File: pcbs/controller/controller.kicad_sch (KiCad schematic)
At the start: 4 parts, among them J1 Conn_01x11, J2 Conn_01x02, J3 Conn_01x02, U1 XIAO-nRF52840-SMD

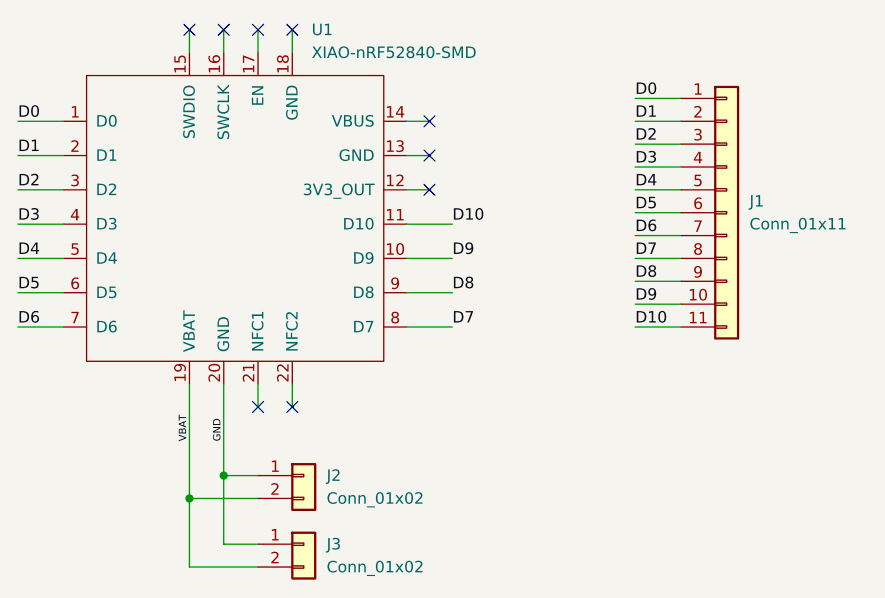
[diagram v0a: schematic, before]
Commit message: Route the controller board
Power on B.Cu (0.5 mm): J2 / J3 to the XIAO battery pads (U1-19 VBAT,
U1-20 GND), clear of B.Cu keepout rule areas (r 3) for the lid
pedestals under H1-H4.

Signals on F.Cu (0.25 mm), all single layer. The H1 screw head blocks
the outside of the top three left pins, and the B.Cu power traces cross
under the XIAO, so D0-D2 run under the module and enter J1 from behind.
D3-D6 and D7-D10 run outside the XIAO and enter J1 from the front,
under the connector body. J1 is reassigned to suit: pins 1-11 =
D6 D5 D4 D3 D2 D1 D0 D10 D9 D8 D7, so with a straight cable
D0-D6 = C0-C6 and D7-D10 = R0-R3.

Also reapply the controller Edge.Cuts after the 6.25-degree tilt
change.

Co-Authored-By: Claude Opus 5.5 <noreply@anthropic.com>
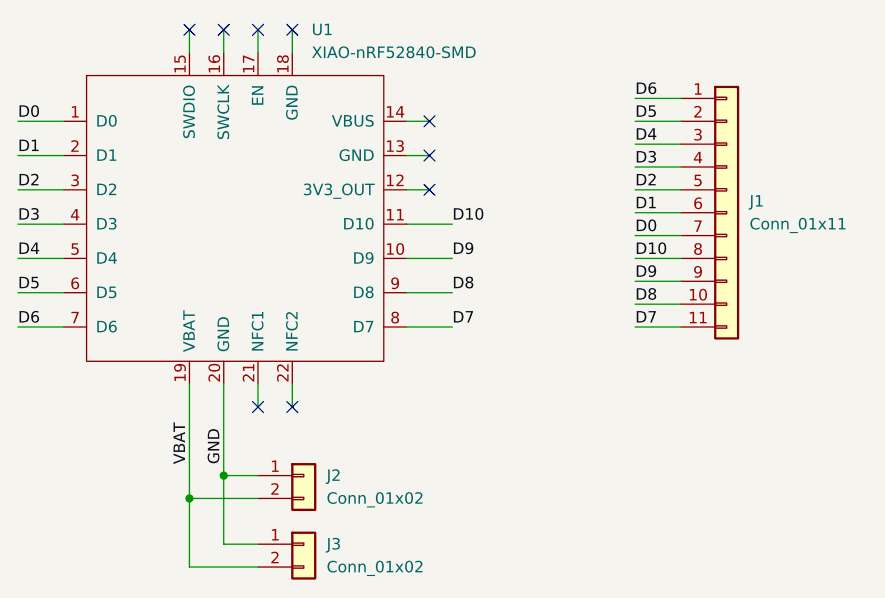
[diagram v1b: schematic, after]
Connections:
- net D0: now also J1.7 (Pin_7); no longer J1.1 (Pin_1)
- net D1: now also J1.6 (Pin_6); no longer J1.2 (Pin_2)
- net D10: now also J1.8 (Pin_8); no longer J1.11 (Pin_11)
- net D2: now also J1.5 (Pin_5); no longer J1.3 (Pin_3)
- net D4: now also J1.3 (Pin_3); no longer J1.5 (Pin_5)
- net D5: now also J1.2 (Pin_2); no longer J1.6 (Pin_6)
- net D6: now also J1.1 (Pin_1); no longer J1.7 (Pin_7)
- net D7: now also J1.11 (Pin_11); no longer J1.8 (Pin_8)
- net D8: now also J1.10 (Pin_10); no longer J1.9 (Pin_9)
- net D9: now also J1.9 (Pin_9); no longer J1.10 (Pin_10)
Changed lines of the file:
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@@
+		)
+	)
+	(label "GND"
+		(at 60.96 90.17 90)
+		(effects
+			(font
+				(size 1.27 1.27)
+			)
+			(justify left bottom)
 		)
 	)
@@
 		)
 	)
-	(label "D6"
+	(label "D0"
 		(at 106.68 64.77 0)
 		(effects
@@
 		)
 	)
-	(label "D10"
+	(label "VBAT"
+		(at 57.15 90.17 90)
+		(effects
+			(font
+				(size 1.27 1.27)
+			)
+			(justify left bottom)
+		)
+	)
+	(label "D7"
 		(at 106.68 74.93 0)
 		(effects
@@
 		)
 	)
-	(label "D2"
+	(label "D4"
 		(at 106.68 54.61 0)
 		(effects
@@
 		)
 	)
-	(label "D0"
+	(label "D6"
 		(at 106.68 49.53 0)
 		(effects
@@
 		)
 	)
-	(label "D4"
+	(label "D2"
 		(at 106.68 59.69 0)
 		(effects
@@
 		)
 	)
-	(label "D8"
+	(label "D9"
 		(at 106.68 69.85 0)
 		(effects
@@
 		)
 	)
+	(label "D1"
+		(at 106.68 62.23 0)
+		(effects
+			(font
+				(size 1.27 1.27)
+			)
+			(justify left bottom)
+		)
+	)
+	(label "D8"
+		(at 106.68 72.39 0)
+		(effects
+			(font
+				(size 1.27 1.27)
+			)
+			(justify left bottom)
+		)
+	)
 	(label "D5"
-		(at 106.68 62.23 0)
-		(effects
-			(font
-				(size 1.27 1.27)
-			)
-			(justify left bottom)
-		)
-	)
-	(label "VBAT"
-		(at 57.15 87.63 90)
-		(effects
-			(font
-				(size 0.8128 0.8128)
-			)
-			(justify left bottom)
-		)
-	)
-	(label "D9"
-		(at 106.68 72.39 0)
-		(effects
-			(font
-				(size 1.27 1.27)
-			)
-			(justify left bottom)
-		)
-	)
-	(label "D1"
 		(at 106.68 52.07 0)
 		(effects
@@
 		)
 	)
-	(label "D7"
+	(label "D10"
 		(at 106.68 67.31 0)
 		(effects
@@
 			)
 			(justify left bottom)
-		)
-	)
-	(label "GND"
-		(at 60.96 87.63 90)
-		(effects
-			(font
-				(size 0.8128 0.8128)
-			)
-			(justify left bottom)
